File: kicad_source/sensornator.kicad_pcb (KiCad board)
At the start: 2 copper layers, 78 x 53 mm, 71 parts, among them CN1 ARDUINO, CN2 SM04B-SRSS-TB, CN3 SM04B-GHS-TB, CN4 SM04B-GHS-TB, CON1 Micro_SDCard, P1 USB_OTG, Q1 2N7002, Q2 2N7002, Q3 BC847, Q4 BC847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

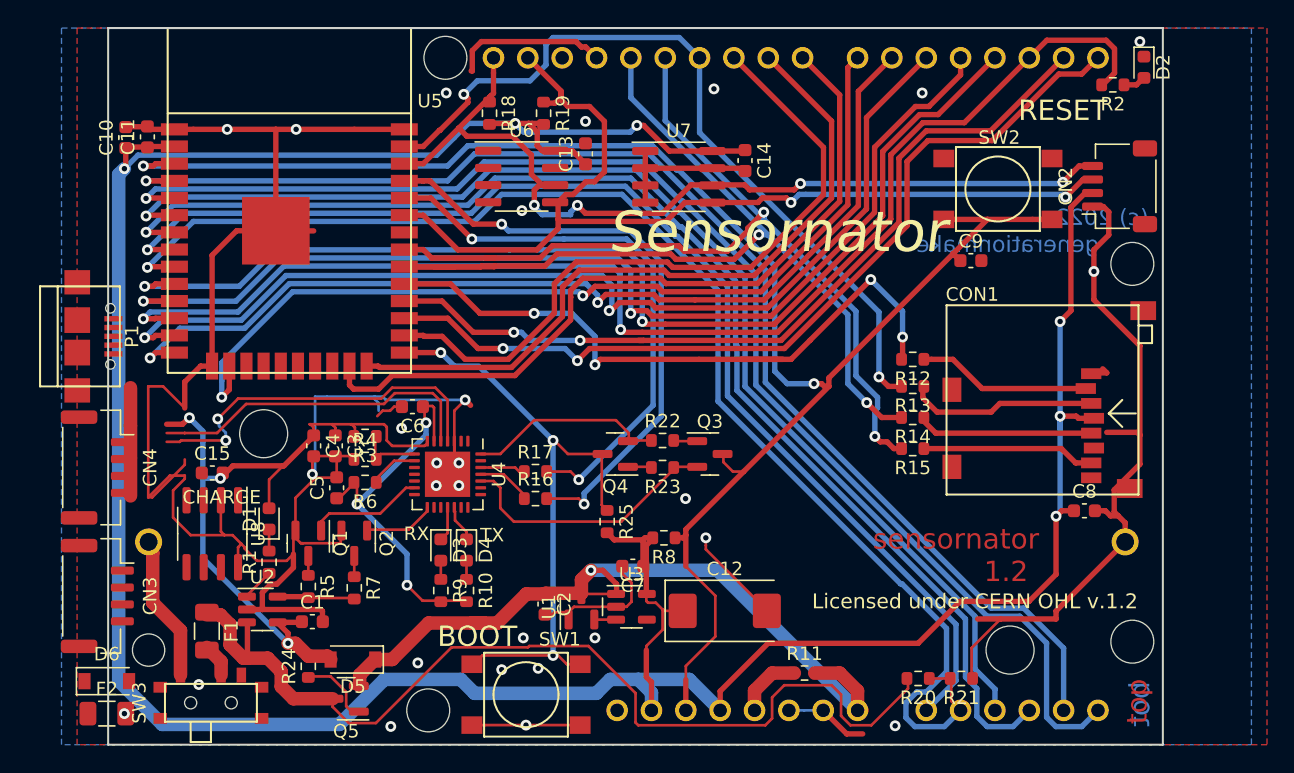
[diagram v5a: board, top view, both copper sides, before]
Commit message: added usb c connector
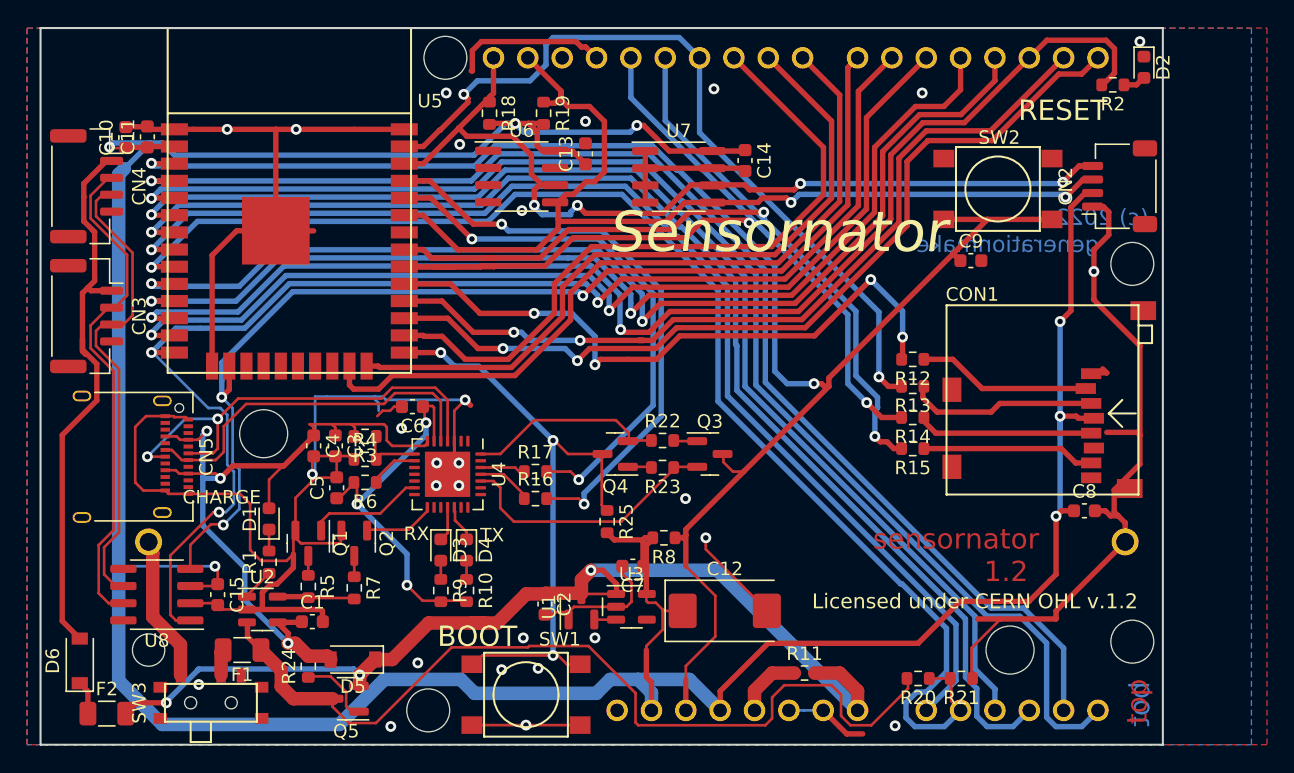
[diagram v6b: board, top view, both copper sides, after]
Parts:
- removed P1: USB_OTG, CON_wuerth:WE_629105136821
- added CN5: USB_C_Receptacle_USB2.0, Connector_USB:USB_C_Receptacle_Amphenol_12401610E4-2A, F.Cu at (45.9, 108.7)
- moved CN4 20.8 mm to (43.4, 88.7)
- moved CN3 20.7 mm to (43.4, 98.3)
- moved C15 9.01 mm to (53.1, 118.9), turned to -90 degrees
- moved U8 6.09 mm to (48.6, 118.9), turned to 180 degrees
- moved F1 2.95 mm to (54.9, 123.0), turned to 180 degrees
- moved D6 2.50 mm to (42.9, 123.8), turned to 90 degrees
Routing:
- net /CANVCC: track 0.00 -> 42.2 mm
- net /CANH: track 0.00 -> 37.3 mm
- net /CANL: track 0.00 -> 35.0 mm
- net /ARDUINO_6: track 72.8 -> 98.5 mm, vias 2 -> 3
- net VCC: track 60.7 -> 79.6 mm, vias 2 -> 3
- net /ARDUINO_7: track 68.0 -> 83.0 mm, vias 2 -> 3
- net +3V3: track 242.4 -> 256.7 mm, vias 6 -> 7
- net GND: track 262.2 -> 249.4 mm, vias 26 -> 28
- net unconnected-(P1-Pad6): track 8.00 -> 0.00 mm
- net +BATT: track 71.9 -> 65.8 mm
- net Net-(U4-Pad4): track 27.6 -> 33.6 mm
- net VIN: track 55.2 -> 59.8 mm
- net /SPI_CS_SD: track 50.8 -> 47.7 mm
- net /DAC_2: track 80.0 -> 77.4 mm
- net Net-(D6-Pad1): track 0.00 -> 2.50 mm
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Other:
- board size 78 x 53 mm -> 83 x 53 mm

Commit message: added resistors on USB CC
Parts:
- added R26: 5k1, Resistor_SMD:R_0603_1608Metric, F.Cu at (51.1, 114.9)
- added R27: 5k1, Resistor_SMD:R_0603_1608Metric, F.Cu at (52.6, 104.8)
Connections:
- net Net-(U4-Pad4) renamed /USB and Power/USBDP
- net Net-(U4-Pad5) renamed /USB and Power/USBDM
- CN5 pad A5: unconnected-(CN5-PadA5) -> /USB and Power/CC1
- CN5 pad B5: unconnected-(CN5-PadB5) -> /USB and Power/CC2
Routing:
- net /USB and Power/CC2: track 0.00 -> 8.86 mm
- net /USB and Power/CC1: track 0.00 -> 3.84 mm
- net VIN: track 59.8 -> 57.0 mm
- net /ARDUINO_6: track 98.5 -> 100.4 mm
- net /USB and Power/DTR: track 14.7 -> 13.0 mm
- net /USB and Power/USBDP: track 33.6 -> 35.1 mm
- net GND: track 249.4 -> 250.5 mm, vias 28 -> 30
- net RESET: track 123.9 -> 123.2 mm

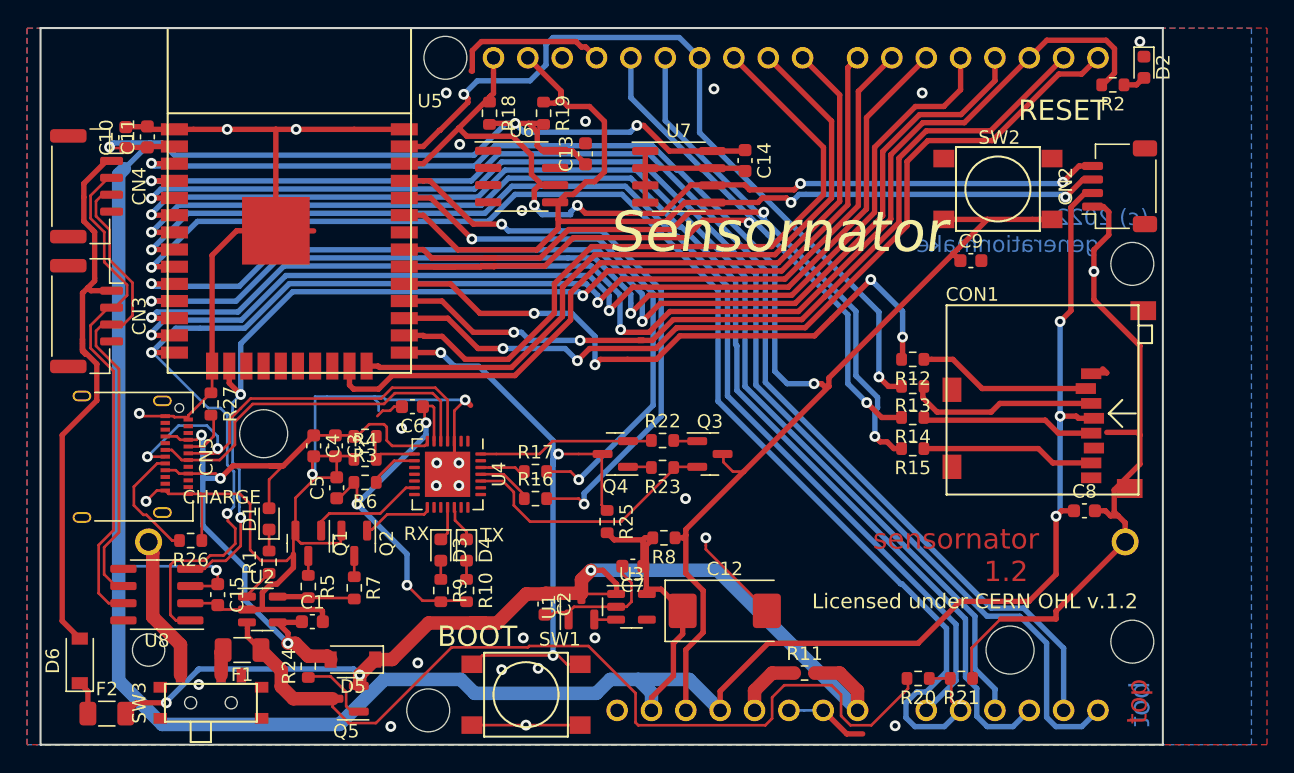
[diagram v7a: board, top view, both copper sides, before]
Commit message: fixedsome drc errors
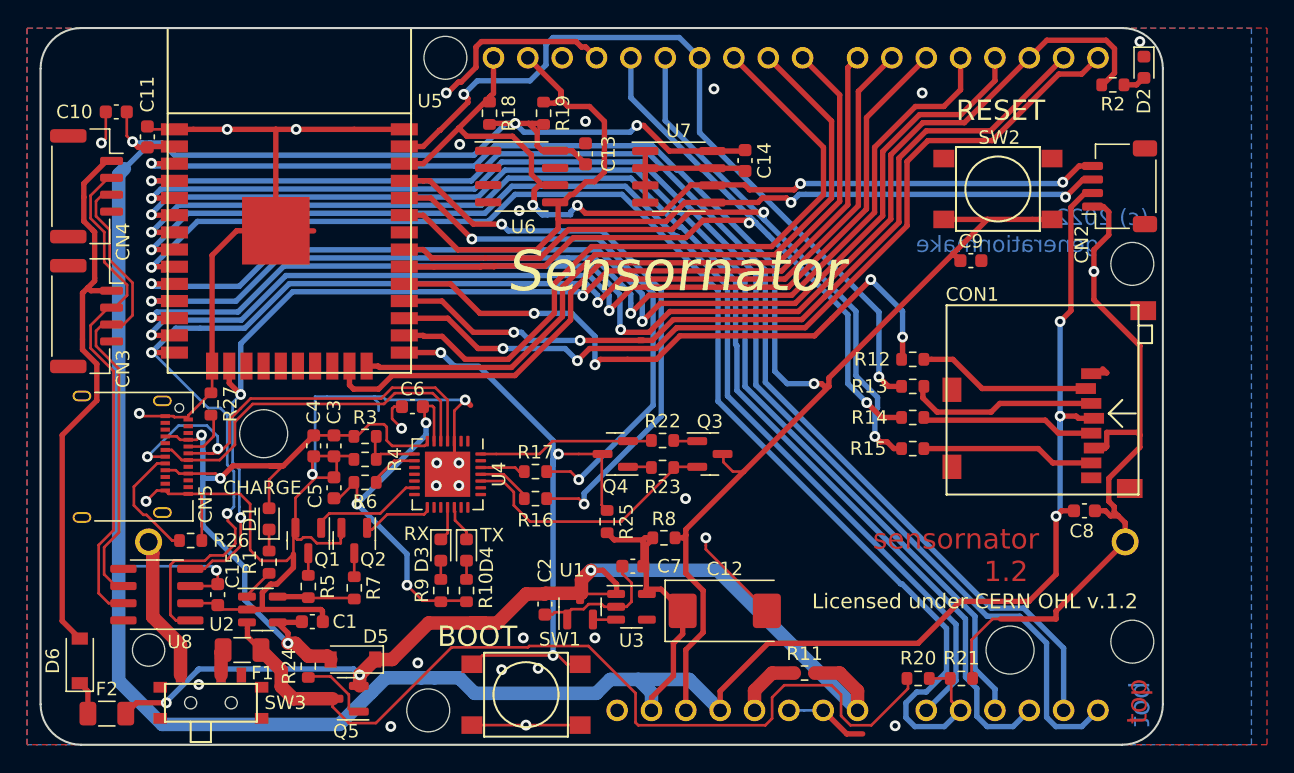
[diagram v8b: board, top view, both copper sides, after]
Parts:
- moved C10 2.02 mm to (45.6, 83.2), turned to 180 degrees
- moved C5 0.20 mm to (61.7, 111.0)
- moved Q1 0.20 mm to (59.8, 114.9)
- moved Q2 0.20 mm to (63.2, 114.9)
- moved C3 0.10 mm to (61.7, 107.9)
- moved U1 0.10 mm to (79.9, 119.8)
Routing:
- net GND: track 250.5 -> 262.3 mm, vias 30 -> 31
- net /I2C_SCL: track 69.3 -> 71.6 mm
- net /ADC_4: track 96.3 -> 94.6 mm
- net /SPI_CLK: track 71.6 -> 70.1 mm
- net +3V3: track 256.6 -> 255.2 mm
- net /CANVCC: track 42.2 -> 41.0 mm
- net /SPI_MISO: track 66.5 -> 65.8 mm
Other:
- outline, holes or cut-outs redrawn
